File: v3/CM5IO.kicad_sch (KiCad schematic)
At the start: 8 parts, among them J1 USB_C_Receptacle_USB2.0

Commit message: Various pcb mods
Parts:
- removed J1: USB_C_Receptacle_USB2.0, Connector_USB:USB_C_Receptacle_GCT_USB4105-xx-A_16P_TopMnt_Horizontal, symbol Connector:USB_C_Receptacle_USB2.0_16P
- added J1: TYPE-C-31-M-12, CM5IO:HRO_TYPE-C-31-M-12, symbol TYPE-C-31-M-12:TYPE-C-31-M-12
- added U6: ~, CM5IO:Raspberry-Pi-5-Compute-Module, symbol cm5_group:CM5_group
- C1, C2: LCSC PN (none) -> C92753
- R1: Field6 (none) -> 0402WGF2201TCE; LCSC PN (none) -> C25879
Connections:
- net +5v: now also J1.A4_B9 (VBUS), J1.B4_A9 (VBUS)
- net CC1: now also J1.A5 (CC1)
- net CC2: now also J1.B5 (CC2)
- net GND: now also J1.A1_B12 (GND), J1.B1_A12 (GND), J1.S1 (SHIELD), J1.S2 (SHIELD), J1.S3 (SHIELD), J1.S4 (SHIELD)
- net USB2_N: now also J1.A7 (DN1), J1.B7 (DN2)
- net USB2_P: now also J1.A6 (DP1), J1.B6 (DP2)

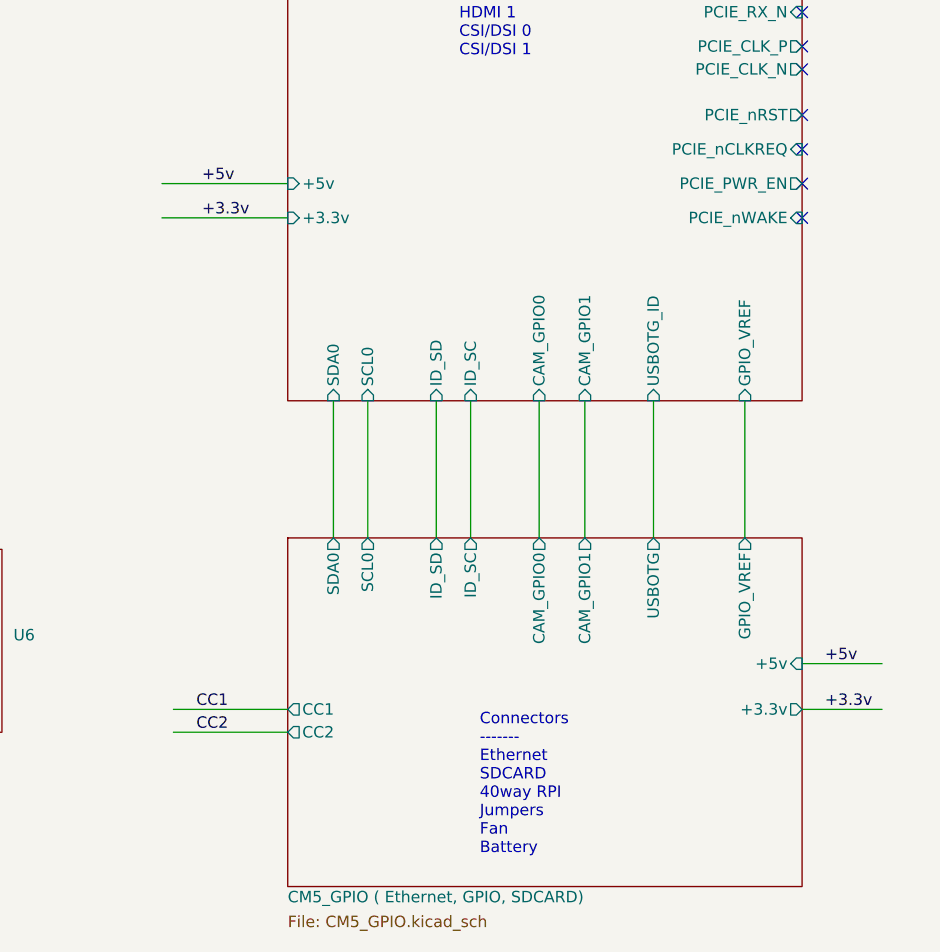
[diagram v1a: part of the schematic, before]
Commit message: convert to CS20 TOF
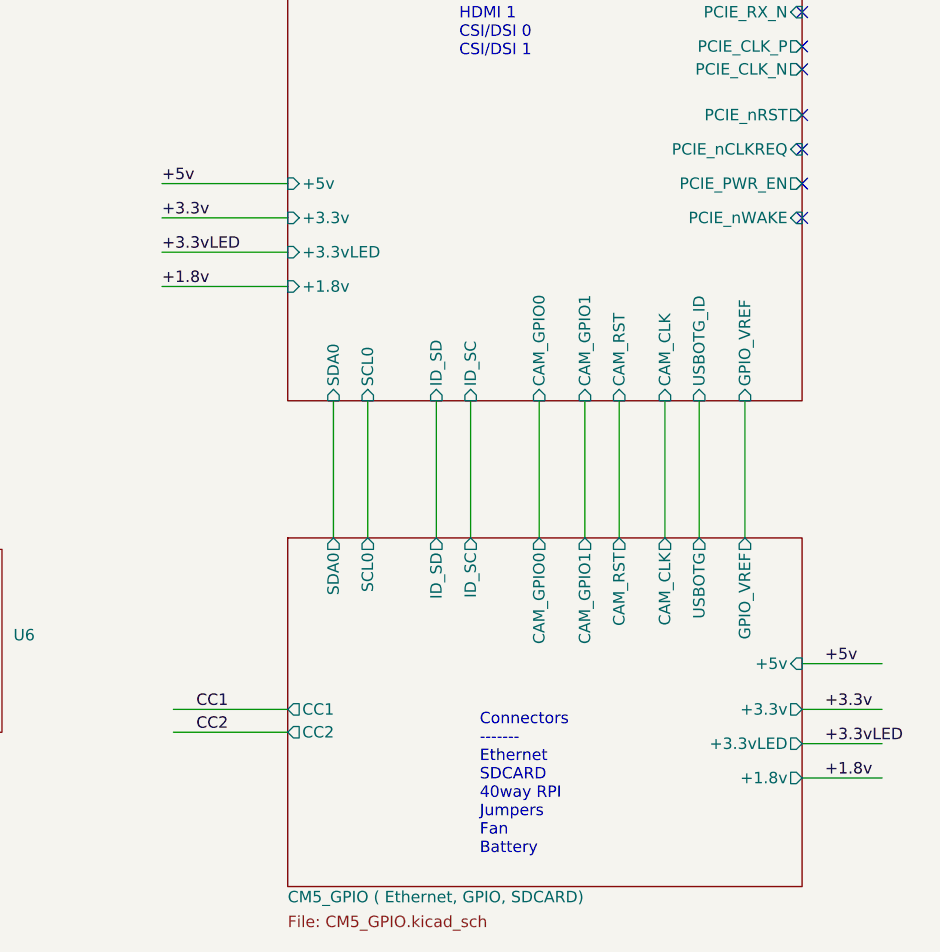
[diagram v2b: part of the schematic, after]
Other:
- sheet CM5_GPIO ( Ethernet, GPIO, SDCARD) ports: added +1.8v, +3.3vLED, CAM_CLK, CAM_RST; removed none
- sheet CM5_HighSpeed ports: added +1.8v, +3.3vLED, CAM_CLK, CAM_RST; removed none
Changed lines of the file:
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@@
+	(wire
+		(pts
+			(xy 166.37 96.52) (xy 166.37 111.76)
+		)
+		(stroke
+			(width 0)
+			(type default)
+		)
+	)
 	(wire
 		(pts
@@
 	(wire
 		(pts
+			(xy 115.57 80.01) (xy 129.54 80.01)
+		)
+		(stroke
+			(width 0)
+			(type default)
+		)
+	)
+	(wire
+		(pts
 			(xy 72.39 80.01) (xy 83.82 80.01)
 		)
@@
 	(wire
 		(pts
+			(xy 129.54 83.82) (xy 115.57 83.82)
+		)
+		(stroke
+			(width 0)
+			(type default)
+		)
+	)
+	(wire
+		(pts
+			(xy 186.69 134.62) (xy 195.58 134.62)
+		)
+		(stroke
+			(width 0)
+			(type default)
+		)
+	)
+	(wire
+		(pts
 			(xy 72.39 80.01) (xy 72.39 82.55)
 		)
@@
 	(wire
 		(pts
-			(xy 170.18 96.52) (xy 170.18 111.76)
+			(xy 175.26 96.52) (xy 175.26 111.76)
+		)
+		(stroke
+			(width 0)
+			(type default)
+		)
+	)
+	(wire
+		(pts
+			(xy 186.69 138.43) (xy 195.58 138.43)
 		)
 		(stroke
@@
 		(pts
 			(xy 72.39 72.39) (xy 83.82 72.39)
+		)
+		(stroke
+			(width 0)
+			(type default)
+		)
+	)
+	(wire
+		(pts
+			(xy 171.45 96.52) (xy 171.45 111.76)
 		)
 		(stroke
@@
 		)
 	)
+	(label "+3.3vLED"
+		(at 115.57 80.01 0)
+		(effects
+			(font
+				(size 1.27 1.27)
+			)
+			(justify left bottom)
+		)
+	)
 	(label "CC2"
 		(at 119.38 133.35 0)
@@
 	)
 	(label "+5v"
-		(at 120.015 72.39 0)
+		(at 115.57 72.39 0)
+		(effects
+			(font
+				(size 1.27 1.27)
+			)
+			(justify left bottom)
+		)
+	)
+	(label "+1.8v"
+		(at 115.57 83.82 0)
+		(effects
+			(font
+				(size 1.27 1.27)
+			)
+			(justify left bottom)
+		)
+	)
+	(label "+3.3vLED"
+		(at 189.23 134.62 0)
+		(effects
+			(font
+				(size 1.27 1.27)
+			)
+			(justify left bottom)
+		)
+	)
+	(label "+1.8v"
+		(at 189.23 138.43 0)
 		(effects
 			(font
@@
 	)
 	(label "+3.3v"
-		(at 120.015 76.2 0)
+		(at 115.57 76.2 0)
 		(effects
 			(font
@@
 		)
 		(pin "USBOTG" output
-			(at 170.18 111.76 90)
+			(at 175.26 111.76 90)
 			(effects
 				(font
@@
 				)
 				(justify left)
+			)
+		)
+		(pin "CAM_RST" output
+			(at 166.37 111.76 90)
+			(effects
+				(font
+					(size 1.27 1.27)
+				)
+				(justify right)
+			)
+		)
+		(pin "CAM_CLK" output
+			(at 171.45 111.76 90)
+			(effects
+				(font
+					(size 1.27 1.27)
+				)
+				(justify right)
+			)
+		)
+		(pin "+1.8v" output
+			(at 186.69 138.43 0)
+			(effects
+				(font
+					(size 1.27 1.27)
+				)
+				(justify right)
+			)
+		)
+		(pin "+3.3vLED" output
+			(at 186.69 134.62 0)
+			(effects
+				(font
+					(size 1.27 1.27)
+				)
+				(justify right)
 			)
 		)
@@
 		)
 		(pin "USBOTG_ID" input
-			(at 170.18 96.52 270)
+			(at 175.26 96.52 270)
 			(effects
 				(font
@@
 			(effects
 				(font
+					(size 1.27 1.27)
+				)
+				(justify left)
+			)
+		)
+		(pin "CAM_RST" input
+			(at 166.37 96.52 270)
+			(effects
+				(font
+					(size 1.27 1.27)
+				)
+				(justify left)
+			)
+		)
+		(pin "CAM_CLK" input
+			(at 171.45 96.52 270)
+			(effects
+				(font
+					(size 1.27 1.27)
+				)
+				(justify left)
+			)
+		)
+		(pin "+1.8v" input
+			(at 129.54 83.82 180)
+			(effects
+				(font
+					(size 1.27 1.27)
+				)
+				(justify left)
+			)
+		)
+		(pin "+3.3vLED" input
+			(at 129.54 80.01 180)
+			(effects
+				(font
